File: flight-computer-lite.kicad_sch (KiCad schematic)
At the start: 8 parts, among them J1 USB_C_Receptacle_USB2.0_16P, J2 Micro_SD_Card_Det2, U1 MS5611-01BA, U2 BME680, U3 LIS3MDL, U4 RP2040, U5 W25Q32JVZP

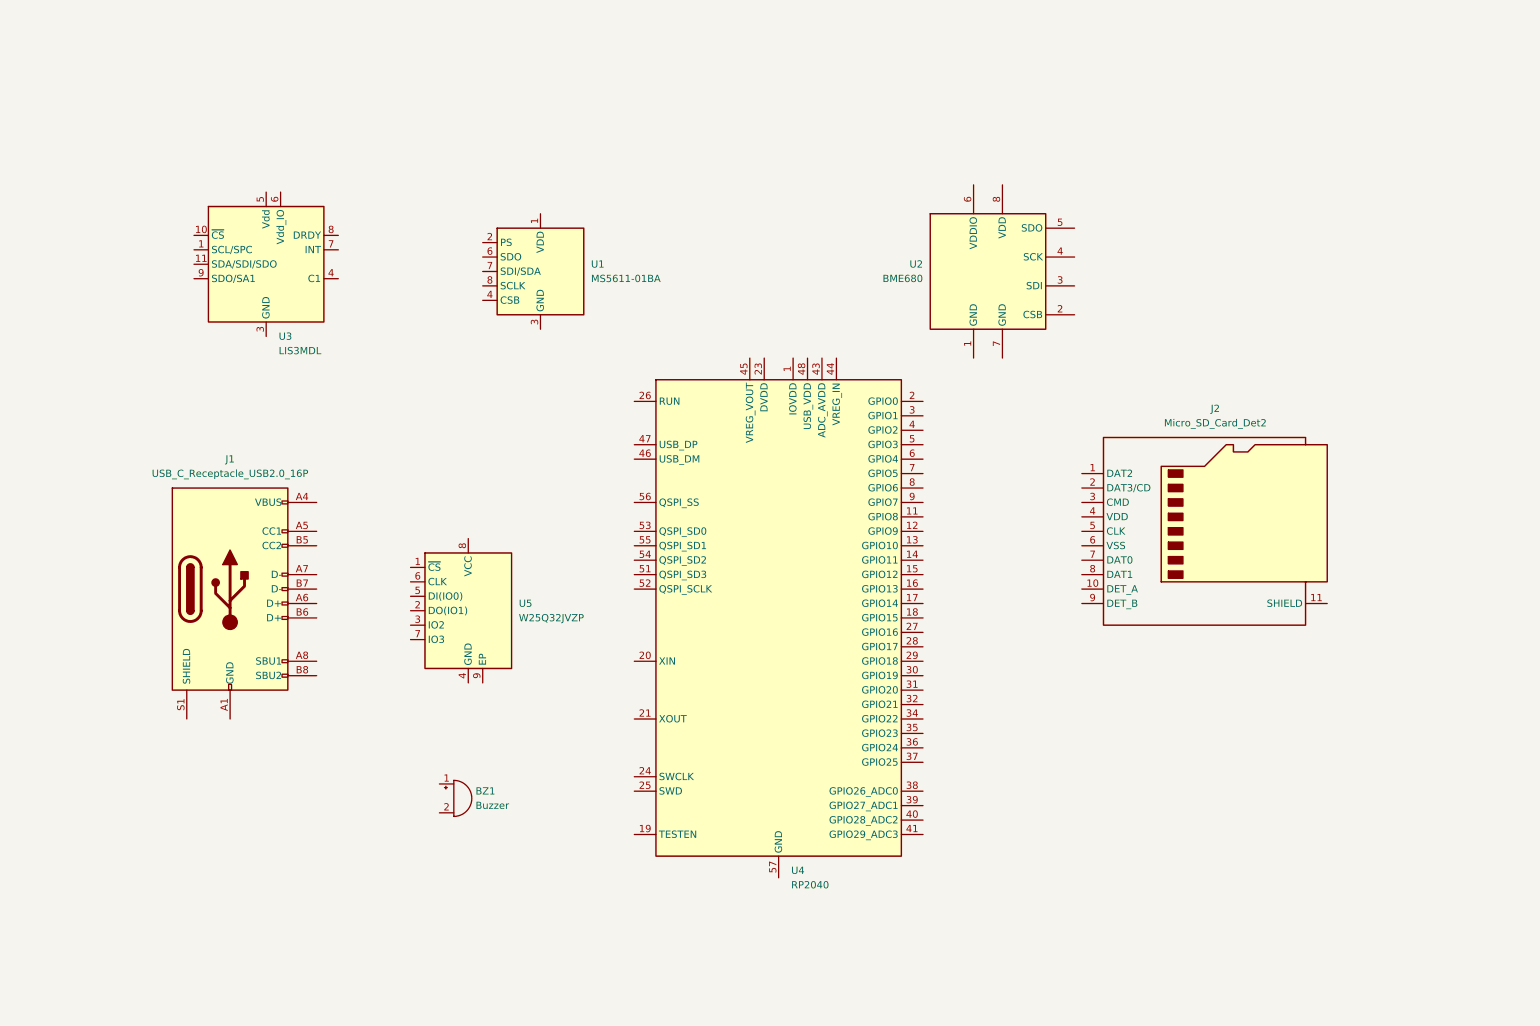
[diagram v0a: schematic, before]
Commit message: Added mounting holes
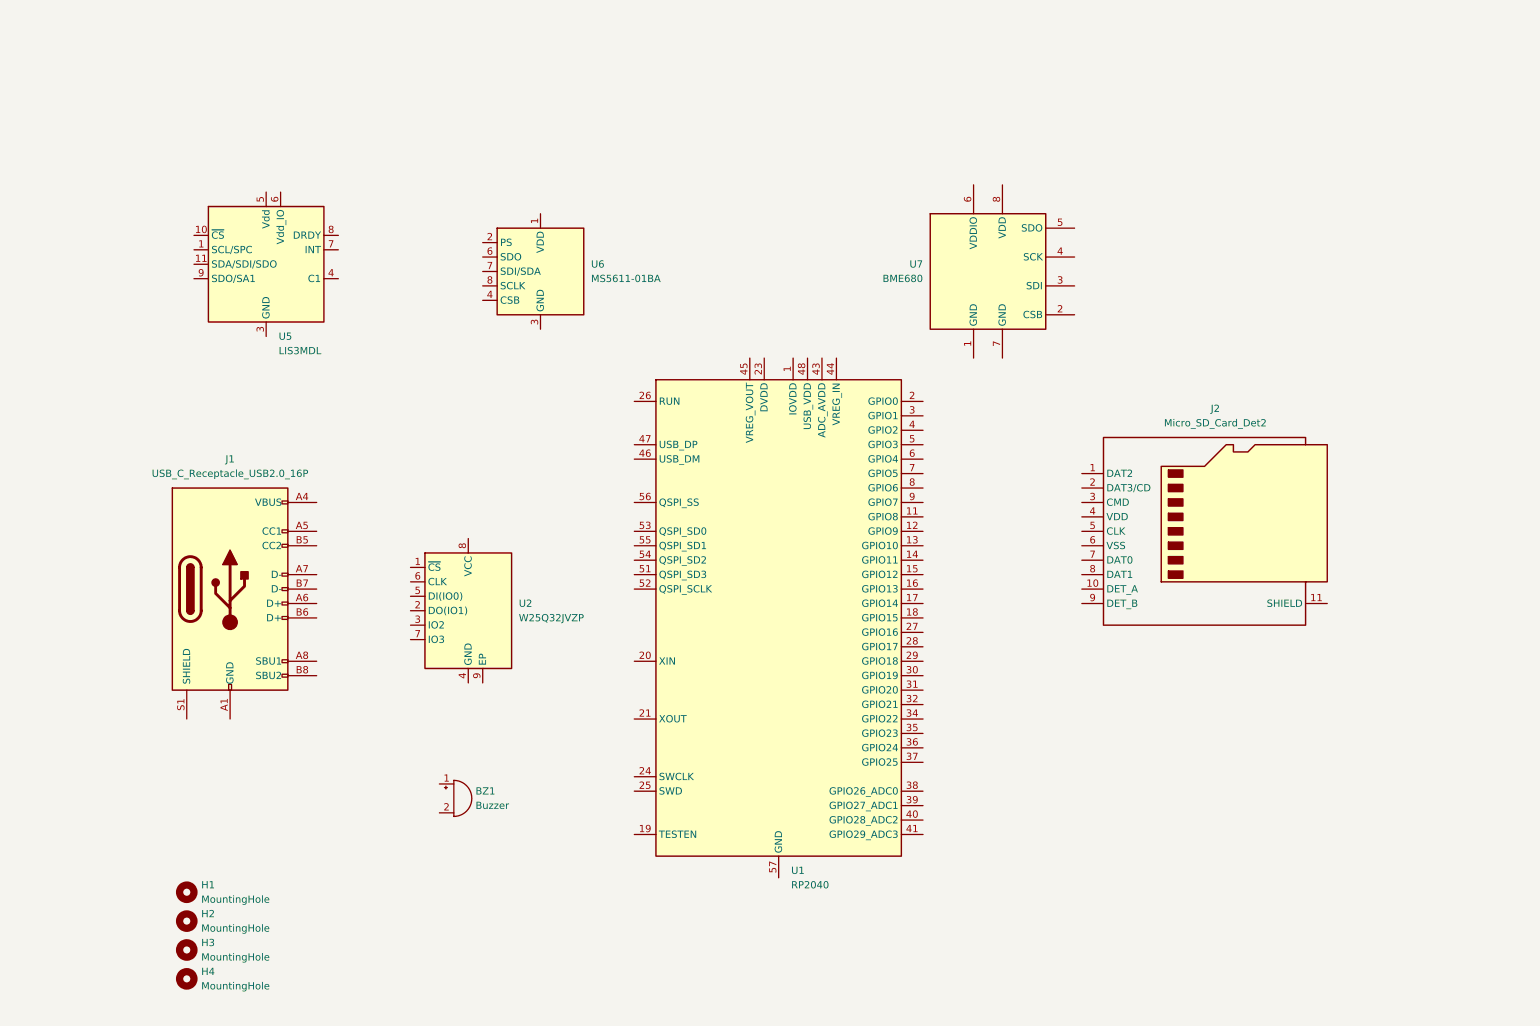
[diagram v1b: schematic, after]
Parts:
- added H1, H2, H3, H4: MountingHole, MountingHole:MountingHole_4.3mm_M4, symbol Mechanical:MountingHole
- renumbered U4 to U1, U5 to U2, U3 to U5, U1 to U6, U2 to U7

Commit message: Changed board surface finish, added GPS
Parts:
- added U8: SAM-M8Q, RF_GPS:ublox_SAM-M8Q, symbol RF_GPS:SAM-M8Q
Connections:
- new net: U8.1 (GND), U8.10 (GND), U8.11 (GND), U8.15 (GND), U8.16 (GND), U8.20 (GND), U8.4 (GND), U8.5 (GND), U8.6 (GND)
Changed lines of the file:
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@@
+	)
+	(symbol
+		(lib_id "RF_GPS:SAM-M8Q")
+		(at 143.51 43.18 0)
+		(unit 1)
+		(exclude_from_sim no)
+		(in_bom yes)
+		(on_board yes)
+		(dnp no)
+		(fields_autoplaced yes)
+		(property "Reference" "U8"
+			(at 145.7041 55.88 0)
+			(effects
+				(font
+					(size 1.27 1.27)
+				)
+				(justify left)
+			)
+		)
+		(property "Value" "SAM-M8Q"
+			(at 145.7041 58.42 0)
+			(effects
+				(font
+					(size 1.27 1.27)
+				)
+				(justify left)
+			)
+		)
+		(property "Footprint" "RF_GPS:ublox_SAM-M8Q"
+			(at 156.21 54.61 0)
+			(effects
+				(font
+					(size 1.27 1.27)
+				)
+				(hide yes)
+			)
+		)
+		(property "Datasheet" "https://www.u-blox.com/sites/default/files/SAM-M8Q_DataSheet_%28UBX-16012619%29.pdf"
+			(at 143.51 43.18 0)
+			(effects
+				(font
+					(size 1.27 1.27)
+				)
+				(hide yes)
+			)
+		)
+		(property "Description" "GPS ublox M8 variant"
+			(at 143.51 43.18 0)
+			(effects
+				(font
+					(size 1.27 1.27)
+				)
+				(hide yes)
+			)
+		)
+		(pin "6"
+		)
+		(pin "13"
+		)
+		(pin "7"
+		)
+		(pin "4"
+		)
+		(pin "11"
+		)
+		(pin "16"
+		)
+		(pin "3"
+		)
+		(pin "1"
+		)
+		(pin "20"
+		)
+		(pin "10"
+		)
+		(pin "19"
+		)
+		(pin "8"
+		)
+		(pin "17"
+		)
+		(pin "2"
+		)
+		(pin "14"
+		)
+		(pin "18"
+		)
+		(pin "12"
+		)
+		(pin "5"
+		)
+		(pin "15"
+		)
+		(pin "9"
+		)
+		(instances
+			(project ""
+				(path "/68fb1519-f2e0-49f5-8b7c-4cc7366600ef"
+					(reference "U8")
+					(unit 1)
+				)
+			)
+		)
 	)
 	(symbol

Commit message: replaced nrnd BME680 with HDC2080
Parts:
- removed U7: BME680, Package_LGA:Bosch_LGA-8_3x3mm_P0.8mm_ClockwisePinNumbering, symbol Sensor:BME680
- added U7: HDC2080, Package_SON:Texas_PWSON-N6, symbol Sensor_Humidity:HDC2080
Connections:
- new net +1V8: U7.5 (VDD)
- new net GND: U7.2 (GND)

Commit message: Changed buzzer partno
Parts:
- BZ1: footprint Buzzer_Beeper:Buzzer_TDK_PS1240P02BT_D12.2mm_H6.5mm -> Buzzer_Beeper:MagneticBuzzer_PUI_SMT-1028-T-2-R
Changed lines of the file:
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@@
 			)
 		)
-		(property "Footprint" "Buzzer_Beeper:Buzzer_TDK_PS1240P02BT_D12.2mm_H6.5mm"
+		(property "Footprint" "Buzzer_Beeper:MagneticBuzzer_PUI_SMT-1028-T-2-R"
 			(at 89.535 152.4 90)
 			(effects

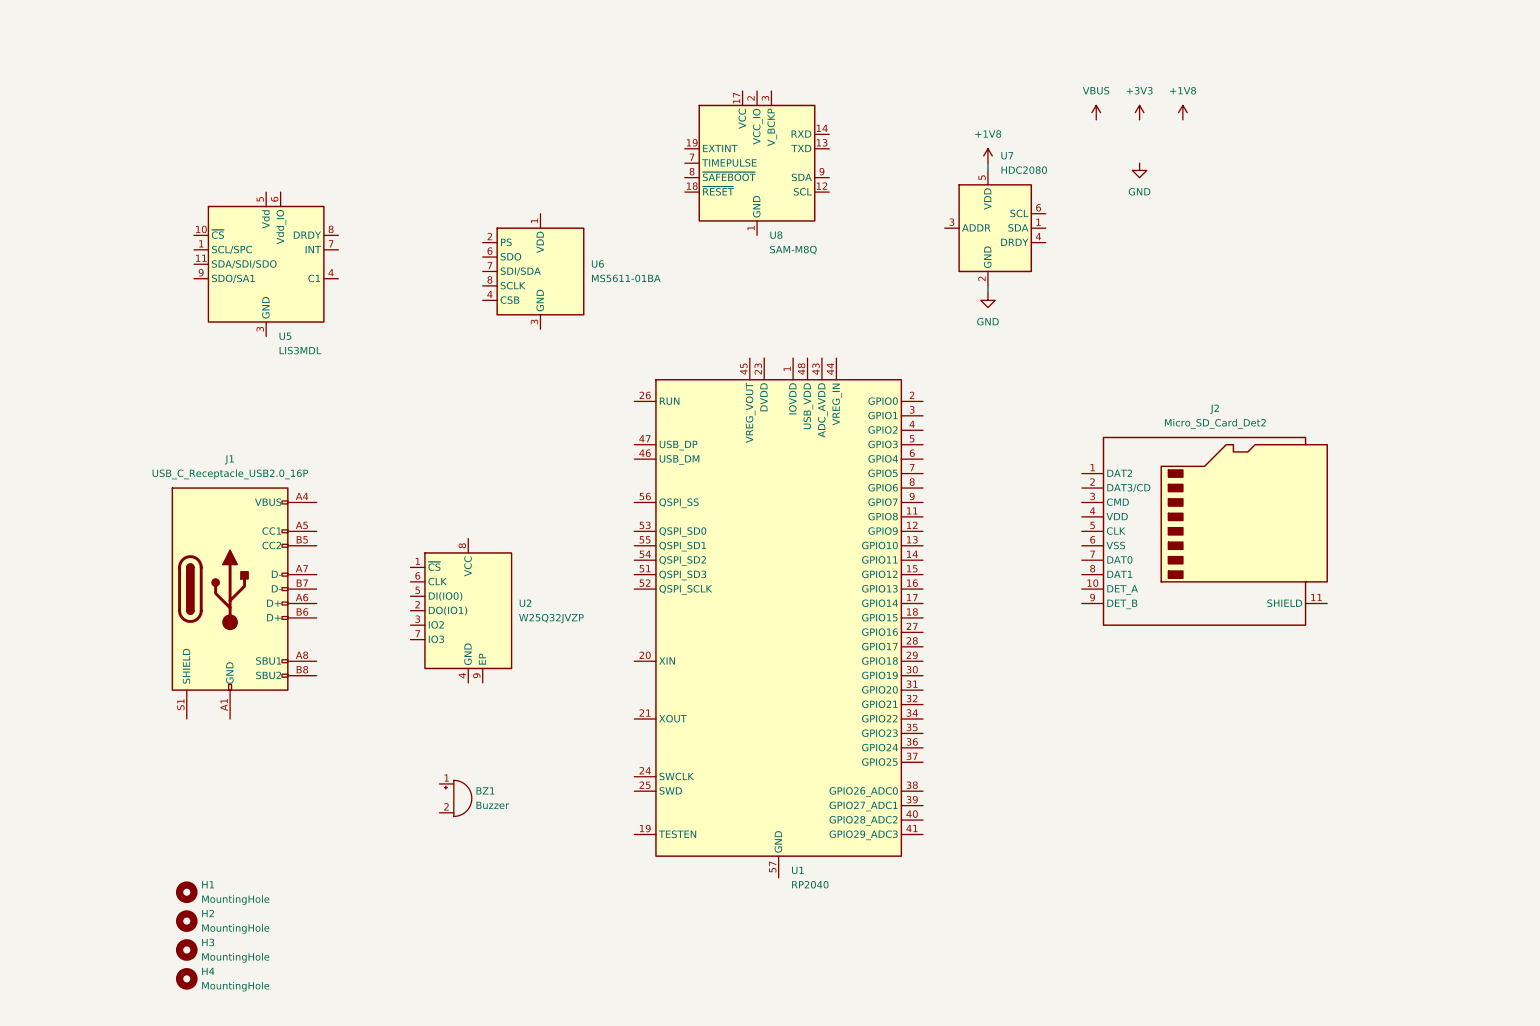
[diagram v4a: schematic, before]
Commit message: Created LRI_partlib
Created a local part library for the project (that can be reused on others in the future).
Added the ICM-42688-P and BMI088 IMUs to it.
Added them to the PCB and reorganized some things.
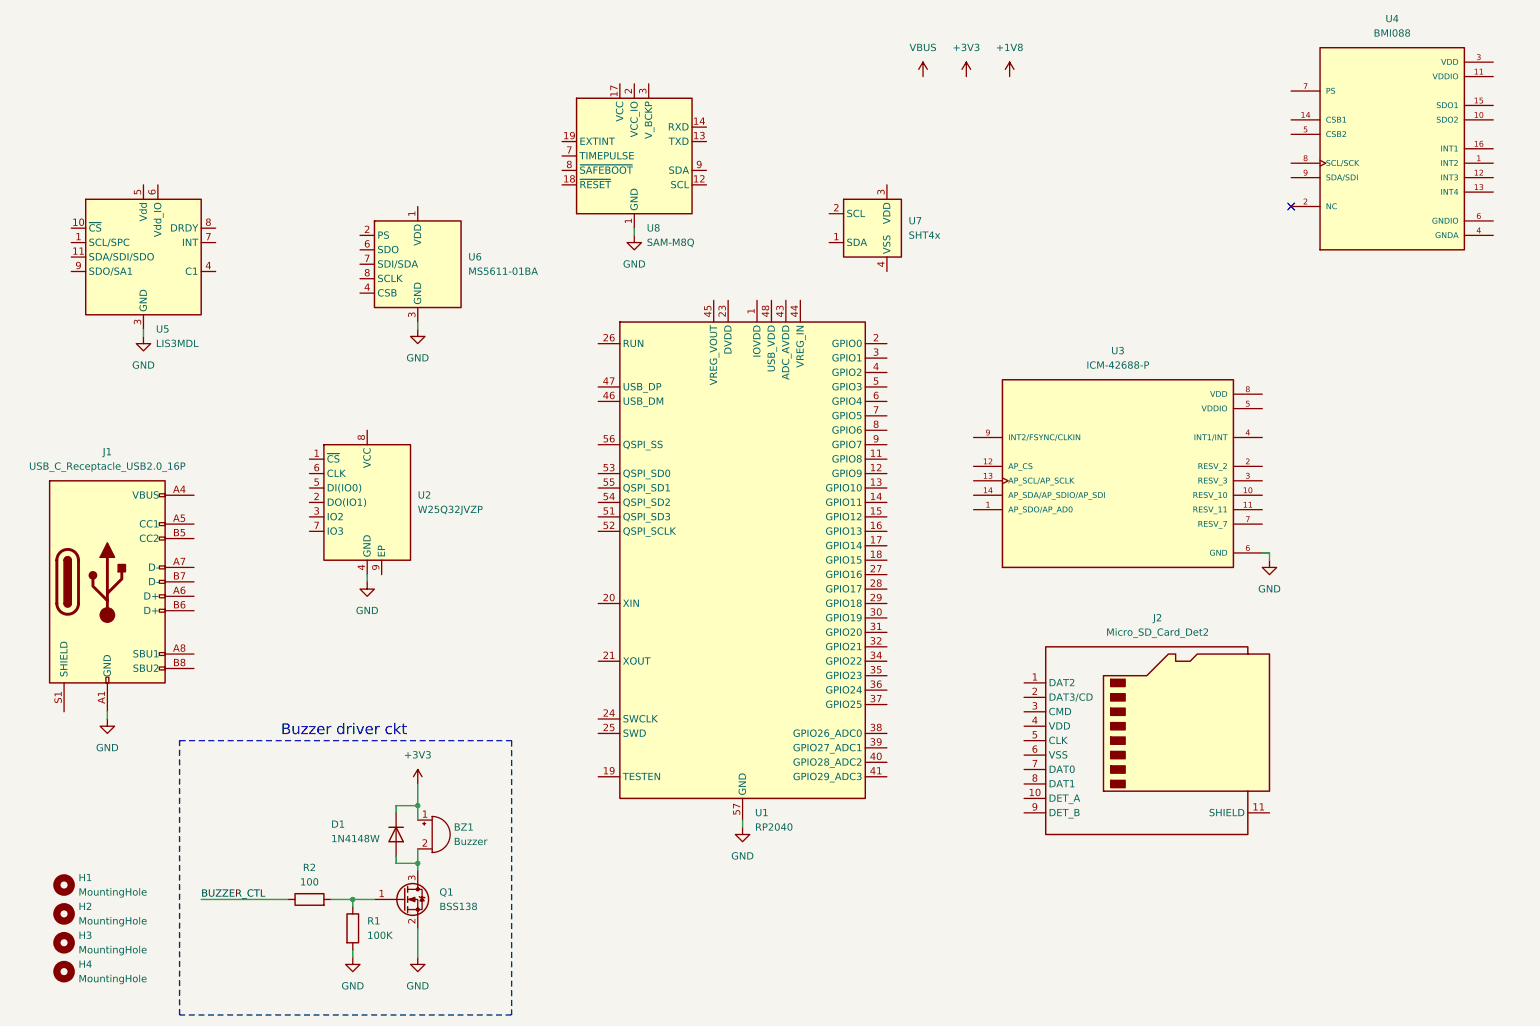
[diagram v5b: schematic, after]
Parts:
- removed U7: HDC2080, Package_SON:Texas_PWSON-N6, symbol Sensor_Humidity:HDC2080
- added D1: 1N4148W, Diode_SMD:D_SOD-323F, symbol Diode:1N4148W
- added Q1: BSS138, Package_TO_SOT_SMD:SOT-23, symbol Transistor_FET:BSS138
- added R1: 100K, Resistor_SMD:R_0805_2012Metric, symbol Device:R
- added R2: 100, Resistor_SMD:R_0805_2012Metric, symbol Device:R
- added U3: ICM-42688-P, LRI_partlib:PQFN50P300X250X97-14N, symbol LRI_partlib:ICM-42688-P
- added U4: BMI088, LRI_partlib:PQFN50P450X300X100-16N, symbol LRI_partlib:BMI088
- added U7: SHT4x, Sensor_Humidity:Sensirion_DFN-4_1.5x1.5mm_P0.8mm_SHT4x_NoCentralPad, symbol Sensor_Humidity:SHT4x
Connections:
- net +3V3: now also BZ1.1 (+), D1.1 (K)
- net GND: now also J1.A1 (GND), J1.A12 (GND), J1.B1 (GND), J1.B12 (GND), U1.57 (GND), U2.4 (GND), U5.12 (GND), U5.2 (GND), U5.3 (GND), U6.3 (GND), U8.1 (GND), U8.10 (GND), U8.11 (GND), U8.15 (GND), U8.16 (GND), U8.20 (GND), U8.4 (GND), U8.5 (GND), U8.6 (GND), Q1.2 (S), R1.2, U3.6 (GND)
- net at BZ1.2 (-): now also D1.2 (A), Q1.3 (D)
- new net: Q1.1 (G), R1.1, R2.2
- new net BUZZER_CTL: R2.1
- no-connect marks 0 -> 1
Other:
- note added: "Buzzer driver ckt"
- moved on the sheet: BZ1, H1, H2, H3, H4, J1, J2, U1, U2, U5, U6, U8

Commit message: Added battery, updated USB
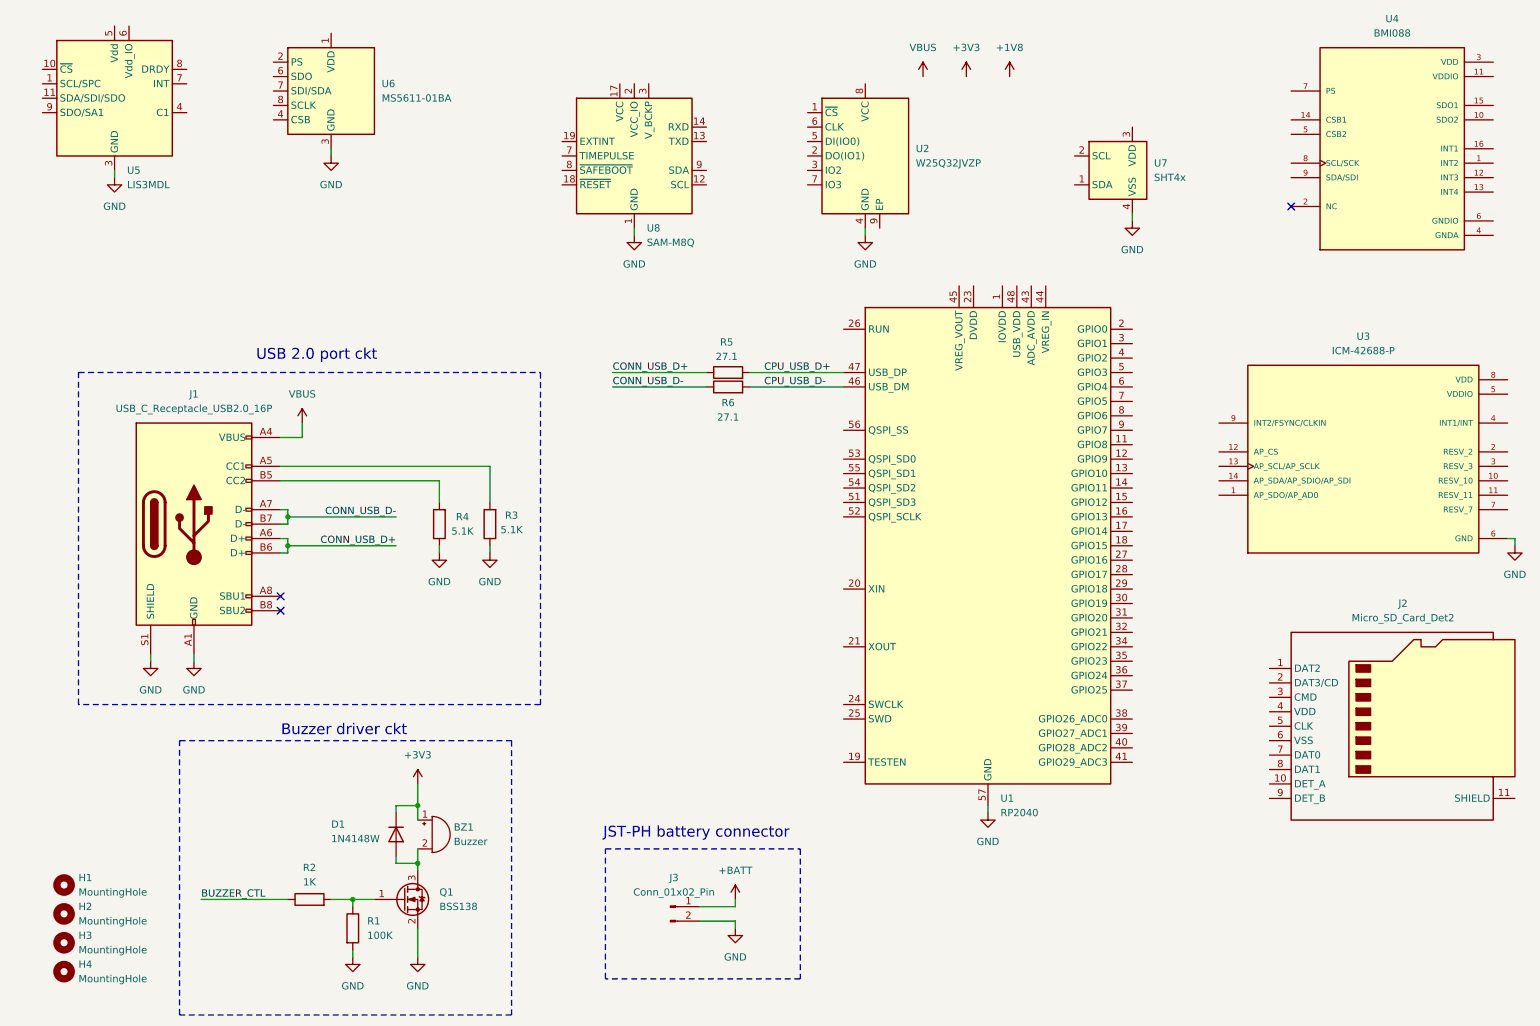
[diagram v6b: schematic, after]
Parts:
- added J3: Conn_01x02_Pin, Connector_JST:JST_PH_S2B-PH-K_1x02_P2.00mm_Horizontal, symbol Connector:Conn_01x02_Pin
- added R3, R4: 5.1K, Resistor_SMD:R_0603_1608Metric, symbol Device:R
- added R5, R6: 27.1, Resistor_SMD:R_0603_1608Metric, symbol Device:R
- J1: footprint Connector_USB:USB_C_Receptacle_HRO_TYPE-C-31-M-12 -> Connector_USB:USB_C_Receptacle_GCT_USB4105-xx-A_16P_TopMnt_Horizontal
- R1: footprint Resistor_SMD:R_0805_2012Metric -> Resistor_SMD:R_0603_1608Metric
- R2: value 100 -> 1K; footprint Resistor_SMD:R_0805_2012Metric -> Resistor_SMD:R_0603_1608Metric
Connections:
- net GND: now also J1.S1 (SHIELD), U7.4 (VSS), J3.2 (Pin_2), R3.1, R4.1
- net VBUS: now also J1.A4 (VBUS), J1.A9 (VBUS), J1.B4 (VBUS), J1.B9 (VBUS)
- net at J1.A5 (CC1): now also R3.2
- net CONN_USB_D+: now reaches J1.A6 (D+)
- net CONN_USB_D+: now also J1.B6 (D+), R5.1
- net CONN_USB_D-: now reaches J1.A7 (D-)
- net CONN_USB_D-: now also J1.B7 (D-), R6.1
- net at J1.B5 (CC2): now also R4.2
- net CPU_USB_D-: now reaches U1.46 (USB_DM)
- net CPU_USB_D-: now also R6.2
- net CPU_USB_D+: now reaches U1.47 (USB_DP)
- net CPU_USB_D+: now also R5.2
- new net +BATT: J3.1 (Pin_1)
- no-connect marks 1 -> 3
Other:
- note added: "JST-PH battery connector"
- note added: "USB 2.0 port ckt"
- moved on the sheet: J1, J2, U1, U2, U3, U5, U6, U7
